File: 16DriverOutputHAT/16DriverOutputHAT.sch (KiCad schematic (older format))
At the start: 15 parts, among them J0 RPi_GPIO, P1 A7 A6 A5 A4 A3 A2 A1 A0 C, P2 C B0 B1 B2 B3 B4 B5 B6 B7, P3 0 1 2, U1 MCP23017, U2 TBD62X83A, U3 TBD62X83A

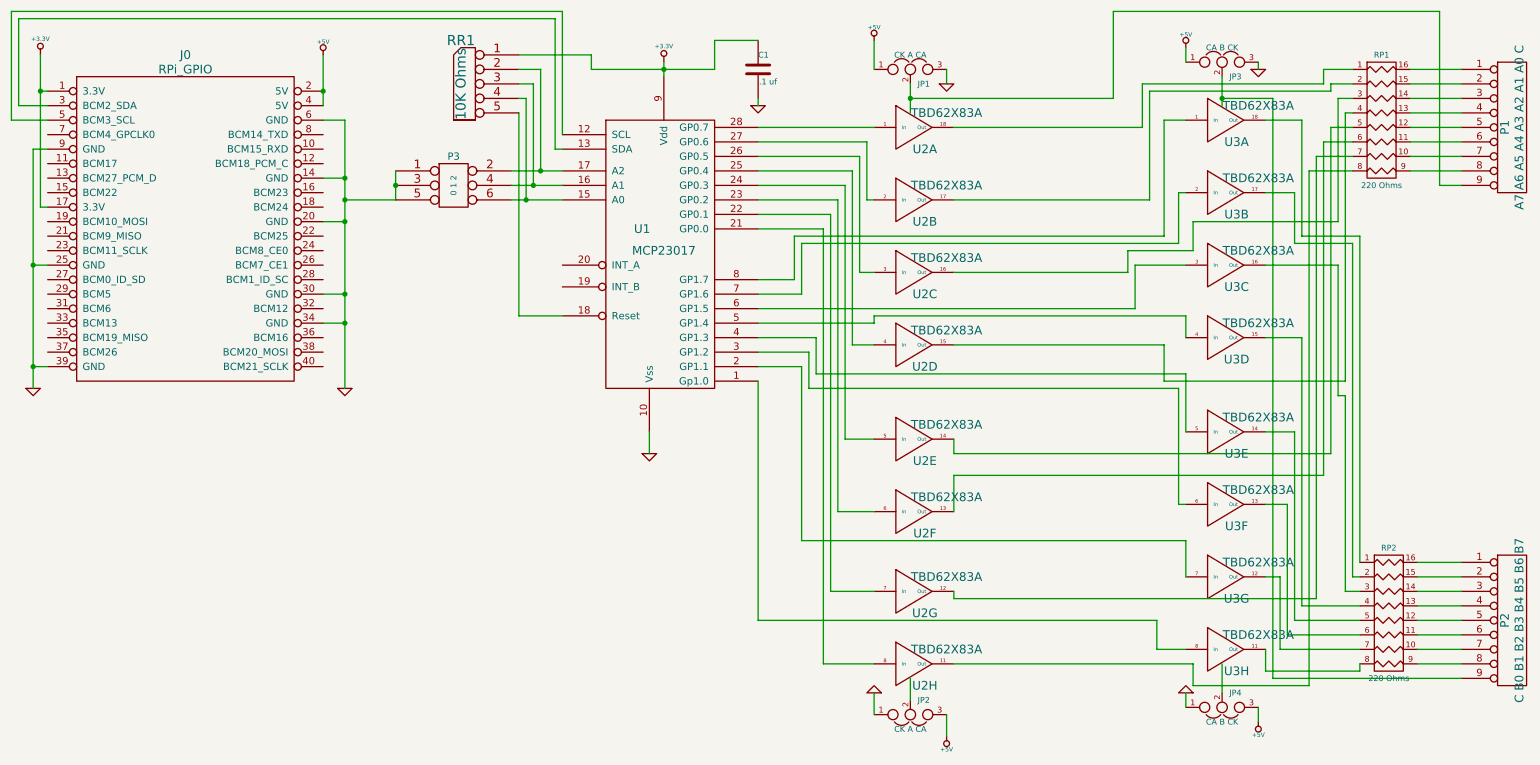
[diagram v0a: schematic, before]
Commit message: Update 16DriverOutputHAT to user a 12V supply for the LEDs, adding a screw terminal for the 12 supply and changing the load resistors to 1.5K.
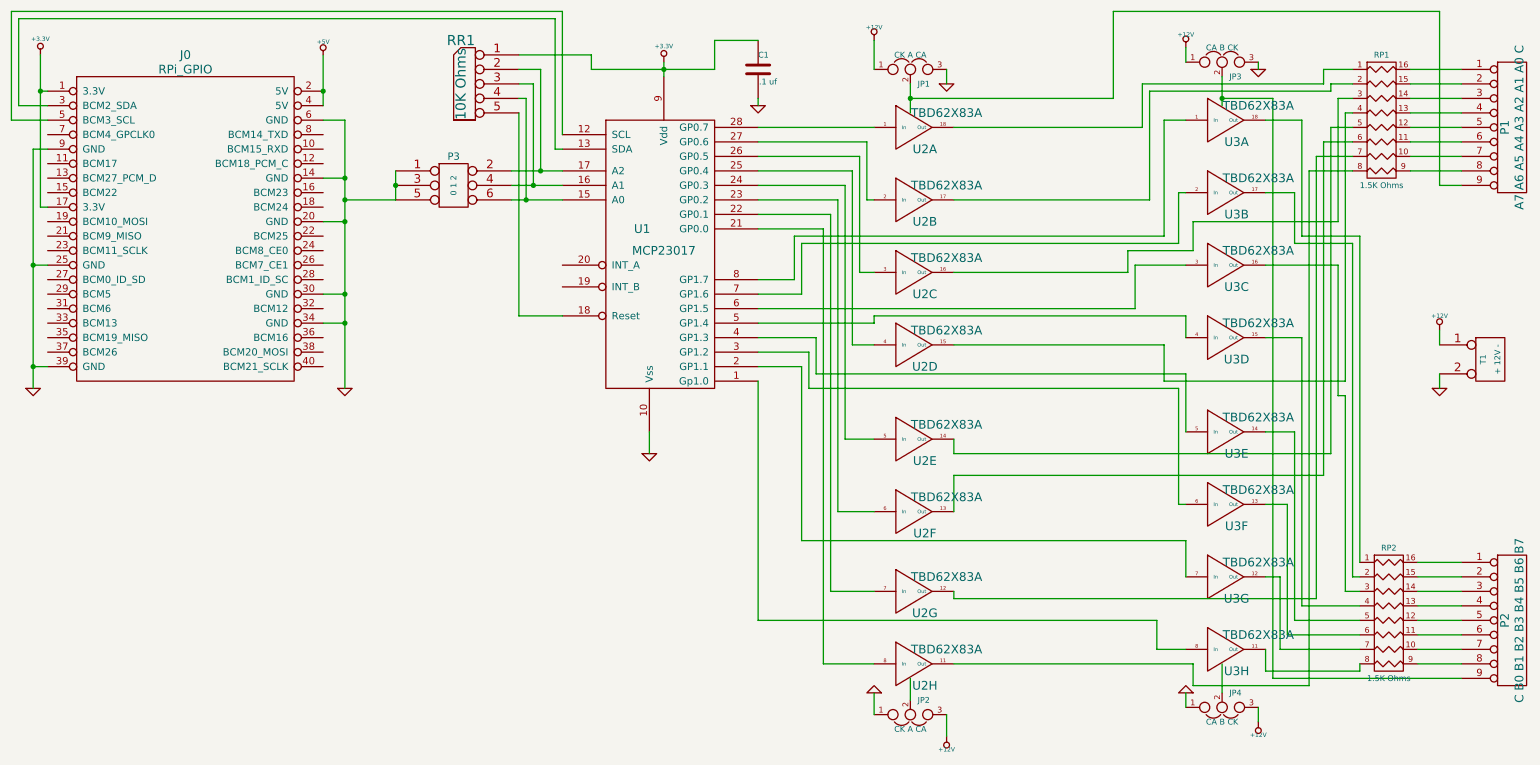
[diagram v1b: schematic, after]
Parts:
- added T1: + 12V -, symbol CONN_2
- RP1, RP2: value 220 Ohms -> 1.5K Ohms
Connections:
- net +5V: no longer JP1.1, JP2.3, JP3.1, JP4.3
- net GND: now also T1.2 (PM)
- new net +12V: JP1.1, JP2.3, JP3.1, JP4.3, T1.1 (P1)
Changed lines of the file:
@@
 Sheet 1 1
 Title ""
-Date "25 feb 2019"
+Date "28 mar 2019"
 Rev ""
 Comp ""
@@
 P 9900 1500
 F 0 "RP1" H 9900 1950 40  0000 C CNN
-F 1 "220 Ohms" H 9900 1050 40  0000 C CNN
+F 1 "1.5K Ohms" H 9900 1050 40  0000 C CNN
 F 2 "~" H 9900 1500 60  0000 C CNN
 F 3 "~" H 9900 1500 60  0000 C CNN
@@
 P 9950 4900
 F 0 "RP2" H 9950 5350 40  0000 C CNN
-F 1 "220 Ohms" H 9950 4450 40  0000 C CNN
+F 1 "1.5K Ohms" H 9950 4450 40  0000 C CNN
 F 2 "~" H 9950 4900 60  0000 C CNN
 F 3 "~" H 9950 4900 60  0000 C CNN
@@
 	9750 5300 9750 5250
 $Comp
-L +5V #PWR01
+L +12V #PWR01
 U 1 1 5C73315D
 P 8550 1000
 F 0 "#PWR01" H 8550 1090 20  0001 C CNN
-F 1 "+5V" H 8550 1090 30  0000 C CNN
+F 1 "+12V" H 8550 1090 30  0000 C CNN
 F 2 "" H 8550 1000 60  0000 C CNN
 F 3 "" H 8550 1000 60  0000 C CNN
@@
 	8550 1100 8550 1000
 $Comp
-L +5V #PWR03
+L +12V #PWR03
 U 1 1 5C7332AE
 P 9050 5650
 F 0 "#PWR03" H 9050 5740 20  0001 C CNN
-F 1 "+5V" H 9050 5740 30  0000 C CNN
+F 1 "+12V" H 9050 5740 30  0000 C CNN
 F 2 "" H 9050 5650 60  0000 C CNN
 F 3 "" H 9050 5650 60  0000 C CNN
@@
 	5600 1350 5600 1400
 $Comp
-L +5V #PWR012
+L +12V #PWR012
 U 1 1 5C733D94
 P 6400 950
 F 0 "#PWR012" H 6400 1040 20  0001 C CNN
-F 1 "+5V" H 6400 1040 30  0000 C CNN
+F 1 "+12V" H 6400 1040 30  0000 C CNN
 F 2 "" H 6400 950 60  0000 C CNN
 F 3 "" H 6400 950 60  0000 C CNN
@@
 $EndComp
 $Comp
-L +5V #PWR015
+L +12V #PWR015
 U 1 1 5C734120
 P 6900 5750
 F 0 "#PWR015" H 6900 5840 20  0001 C CNN
-F 1 "+5V" H 6900 5840 30  0000 C CNN
+F 1 "+12V" H 6900 5840 30  0000 C CNN
 F 2 "" H 6900 5750 60  0000 C CNN
 F 3 "" H 6900 5750 60  0000 C CNN
@@
 	9150 5350 10450 5350
 Connection ~ 8800 1350
+$Comp
+L CONN_2 T1
+U 1 1 5C9C1363
+P 10650 3150
+F 0 "T1" V 10600 3150 40  0000 C CNN
+F 1 "+ 12V -" V 10700 3150 40  0000 C CNN
+F 2 "" H 10650 3150 60  0000 C CNN
+F 3 "" H 10650 3150 60  0000 C CNN
+	1    10650 3150
+	1    0    0    -1
+$EndComp
+$Comp
+L GND #PWR016
+U 1 1 5C9C1379
+P 10300 3350
+F 0 "#PWR016" H 10300 3350 30  0001 C CNN
+F 1 "GND" H 10300 3280 30  0001 C CNN
+F 2 "" H 10300 3350 60  0000 C CNN
+F 3 "" H 10300 3350 60  0000 C CNN
+	1    10300 3350
+	1    0    0    -1
+$EndComp
+$Comp
+L +12V #PWR017
+U 1 1 5C9C1388
+P 10300 2950
+F 0 "#PWR017" H 10300 2900 20  0001 C CNN
+F 1 "+12V" H 10300 3050 30  0000 C CNN
+F 2 "" H 10300 2950 60  0000 C CNN
+F 3 "" H 10300 2950 60  0000 C CNN
+	1    10300 2950
+	1    0    0    -1
+$EndComp
+Wire Wire Line
+	10300 2950 10300 3050
+Wire Wire Line
+	10300 3250 10300 3350
 $EndSCHEMATC
